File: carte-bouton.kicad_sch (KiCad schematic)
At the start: 46 parts, among them J1 Connecteur batterie, J14 Conn_ST_STDC14, J4 Conn_01x04, J5 Conn_01x03, J7 Conn_01x03, Q13 Q_NMOS_GDS, U1 LM317_SOT-223, U3 STM32F401RCTx, U4 LMR16020PDDA, Y1 Crystal_GND24

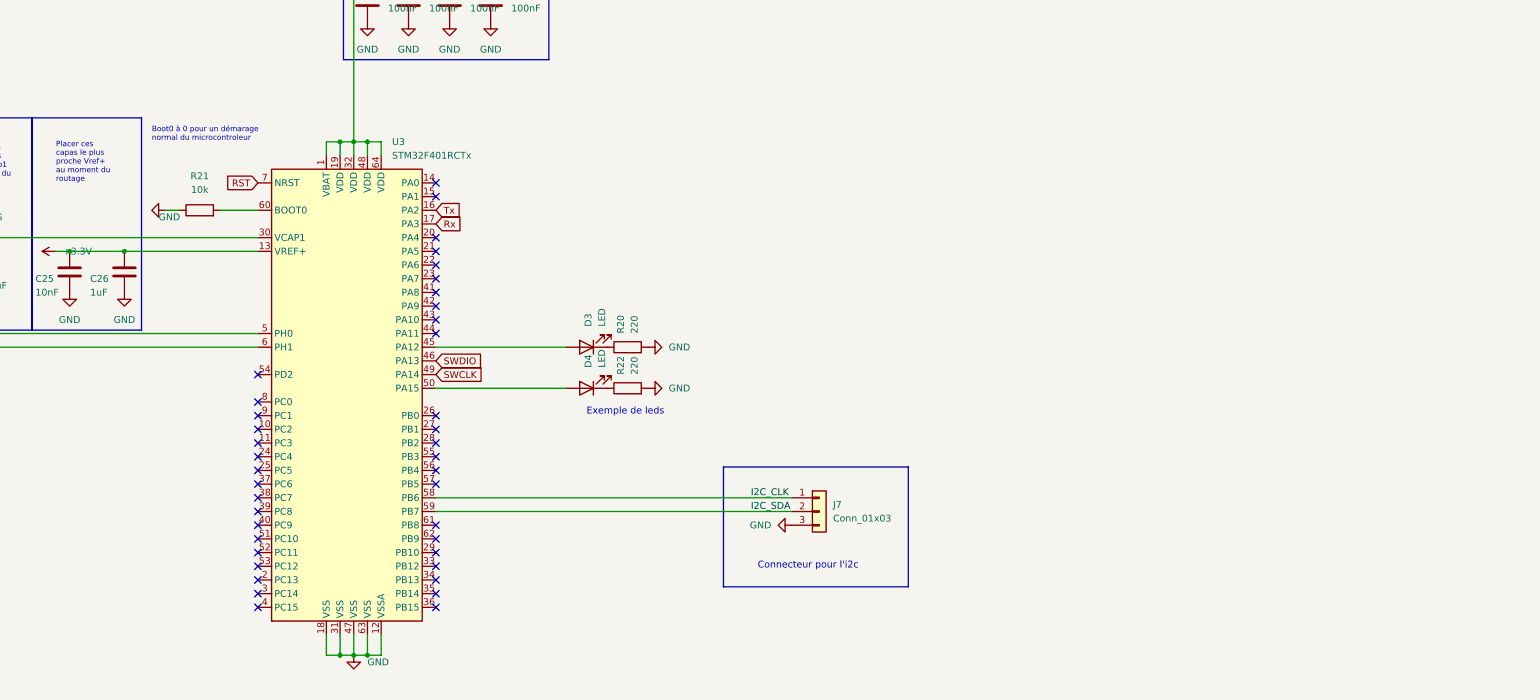
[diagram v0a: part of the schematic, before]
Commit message: Boutons, LEDs sans ecran
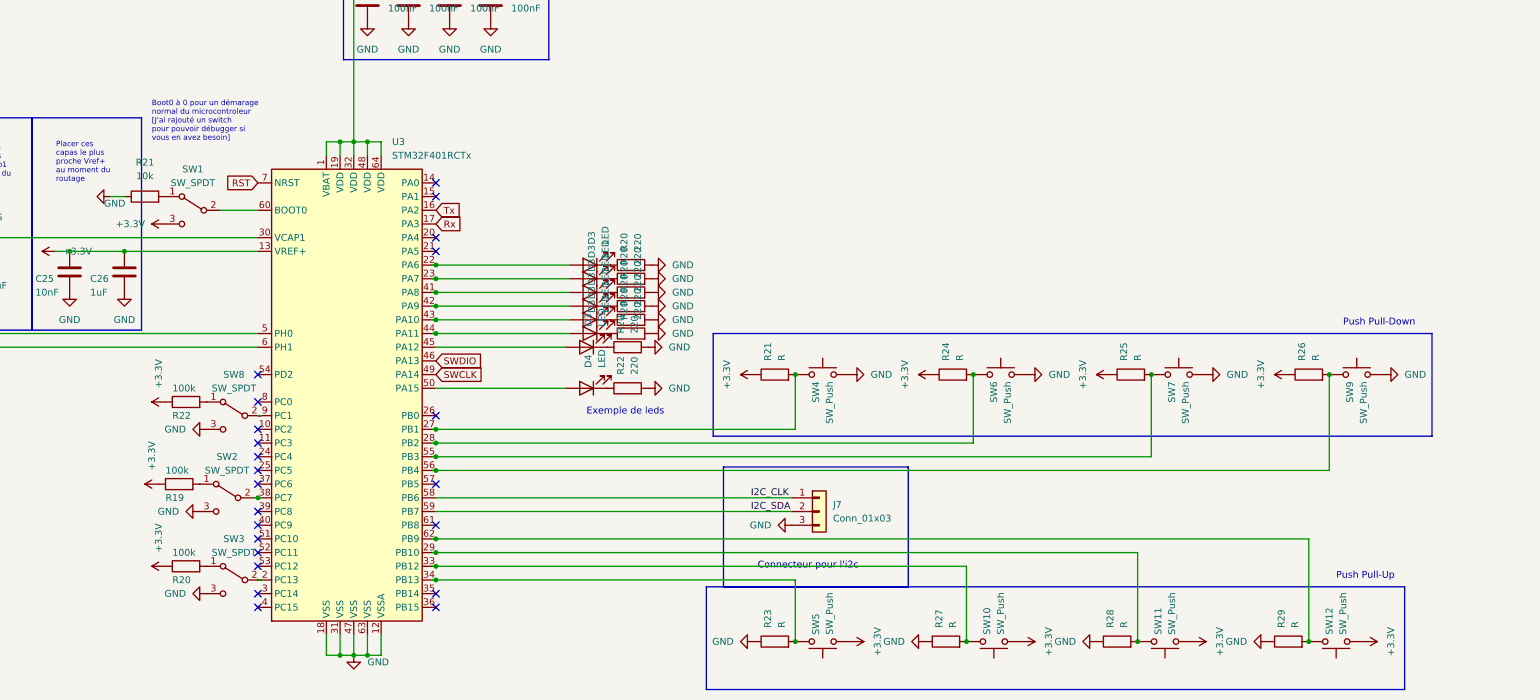
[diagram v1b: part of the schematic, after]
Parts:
- removed R21: 10k, Resistor_SMD:R_0805_2012Metric_Pad1.20x1.40mm_HandSolder, symbol Device:R
- added D3 (x6): LED, LED_SMD:LED_0805_2012Metric_Pad1.15x1.40mm_HandSolder, symbol Device:LED
- added R19, R20, R22: 100k, symbol Device:R
- added R20 (x6): 220, Resistor_SMD:R_0805_2012Metric_Pad1.20x1.40mm_HandSolder, symbol Device:R
- added R21, R23, R24, R25, R26, R27, R28, R29: R, symbol Device:R
- added R21: 10k, Resistor_SMD:R_0805_2012Metric_Pad1.20x1.40mm_HandSolder, symbol Device:R
- added SW1, SW2, SW3, SW8: SW_SPDT, symbol Switch:SW_SPDT
- added SW10, SW11, SW12, SW4, SW5, SW6, SW7, SW9: SW_Push, symbol Switch:SW_Push
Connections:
- net +3.3V: now also R19.1, R20.1, R21.1, R22.1, R24.1, R25.1, R26.1, SW1.3 (C), SW10.1, SW11.1, SW12.1, SW5.1
- net GND: now also R20.2, R20.2, R20.2, R20.2, R20.2, R20.2, R21.1, R23.1, R27.1, R28.1, R29.1, SW2.3 (C), SW3.3 (C), SW4.1, SW6.1, SW7.1, SW8.3 (C), SW9.1
- net at U3.60 (BOOT0): now also SW1.2 (B)
- net at U3.2 (PC13): now also SW3.2 (B)
- net at U3.22 (PA6): now also D3.2 (A)
- net at U3.23 (PA7): now also D3.2 (A)
- net at U3.27 (PB1): now also R21.2, SW4.2
- net at U3.28 (PB2): now also R24.2, SW6.2
- net at U3.29 (PB10): now also R28.2, SW11.2
- net at U3.33 (PB12): now also R27.2, SW10.2
- net at U3.34 (PB13): now also R23.2, SW5.2
- net at U3.38 (PC7): now also SW2.2 (B)
- net at U3.41 (PA8): now also D3.2 (A)
- net at U3.42 (PA9): now also D3.2 (A)
- net at U3.43 (PA10): now also D3.2 (A)
- net at U3.44 (PA11): now also D3.2 (A)
- net at U3.55 (PB3): now also R25.2, SW7.2
- net at U3.56 (PB4): now also R26.2, SW9.2
- net at U3.62 (PB9): now also R29.2, SW12.2
- net at U3.9 (PC1): now also SW8.2 (B)
- new net: R19.2, SW2.1 (A)
- new net: R20.2, SW3.1 (A)
- new net: D3.1 (K), R20.1 (x6)
- new net: R22.2, SW8.1 (A)
- new net: R21.2, SW1.1 (A)
- no-connect marks 45 -> 28
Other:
- note added: "Boot0 à 0 pour un démarage normal du microcontroleur [J'ai rajouté un switch pour pouvoir débugger si vous en avez besoin]"
- note added: "Push Pull-Down"
- note added: "Push Pull-Up"
- note removed: "Boot0 à 0 pour un démarage normal du microcontroleur"

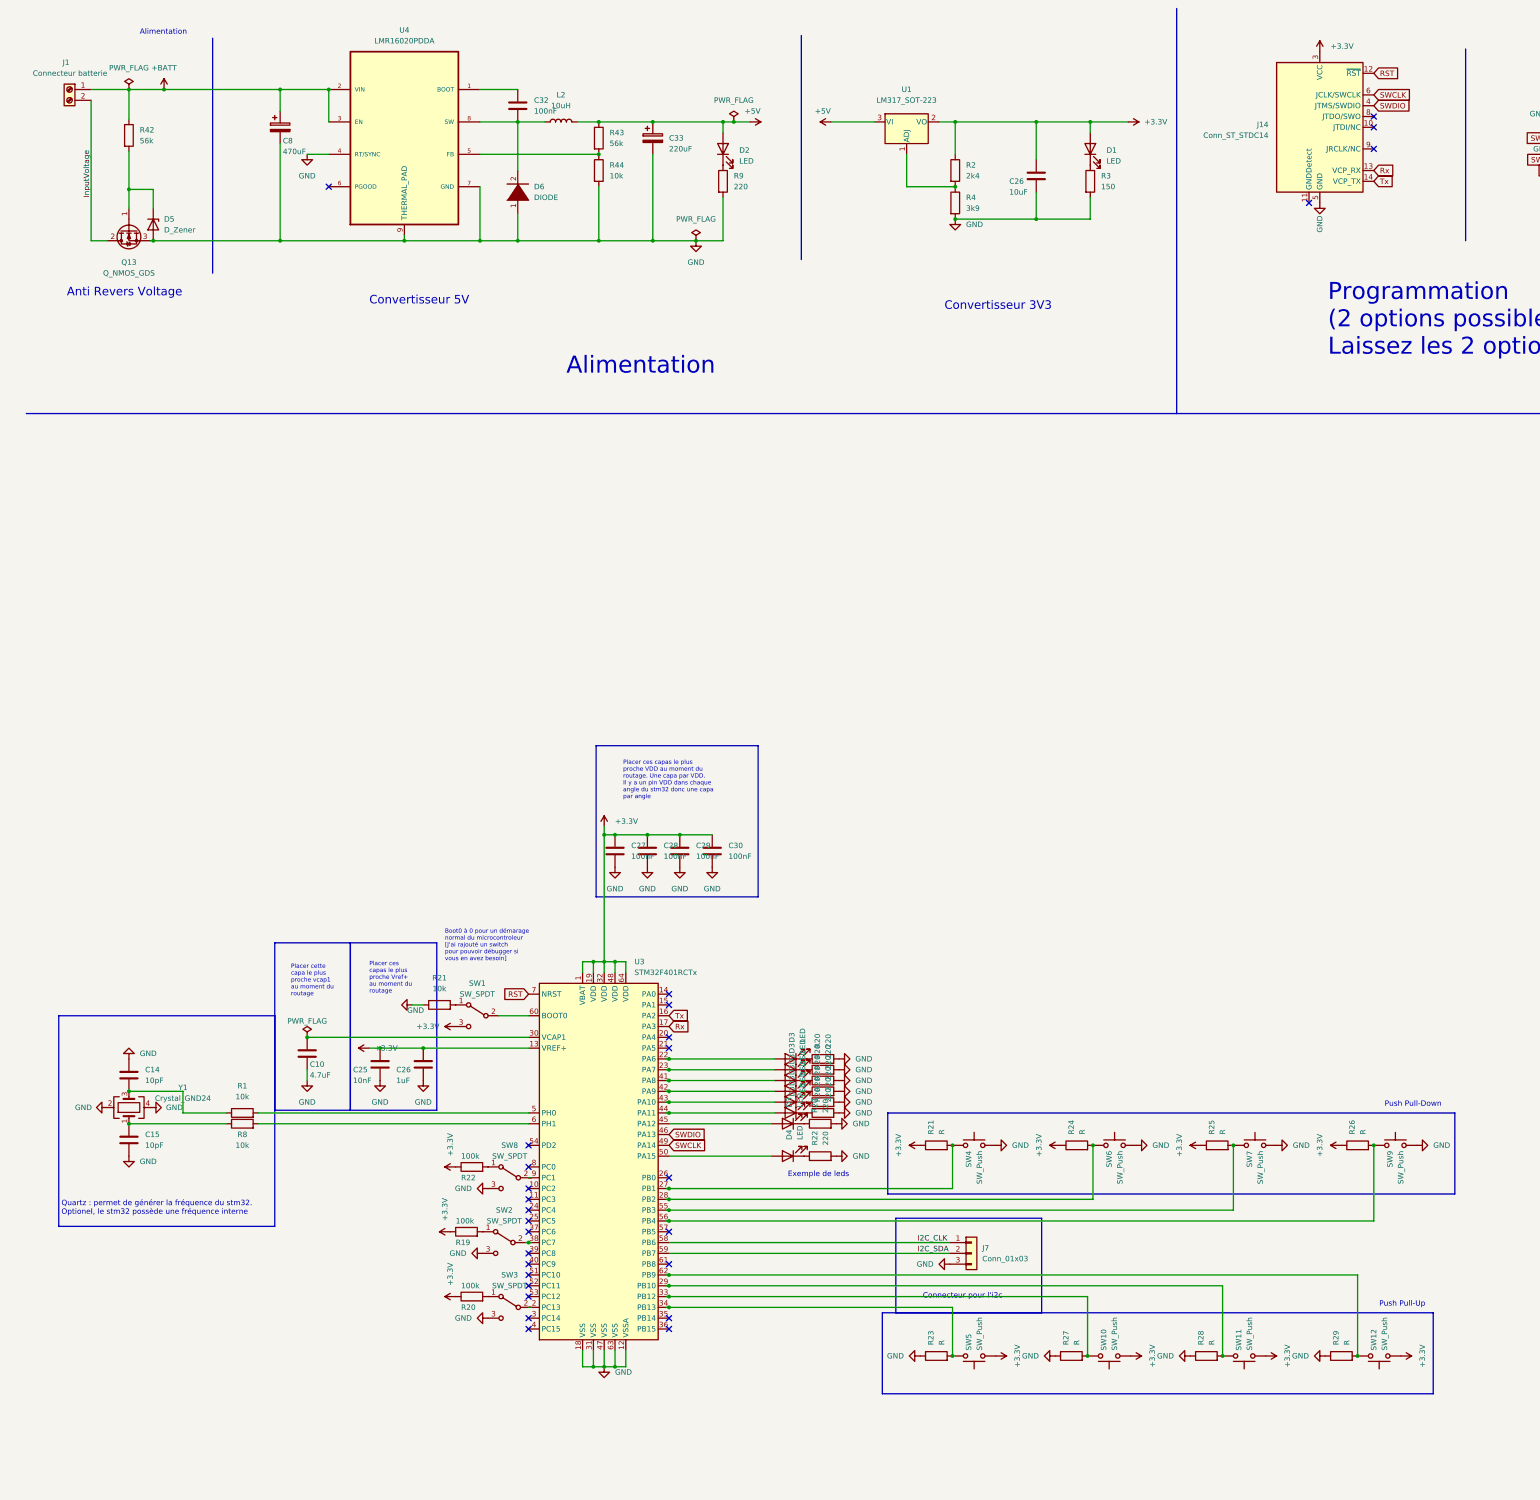
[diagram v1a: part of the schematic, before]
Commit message: modification schémas
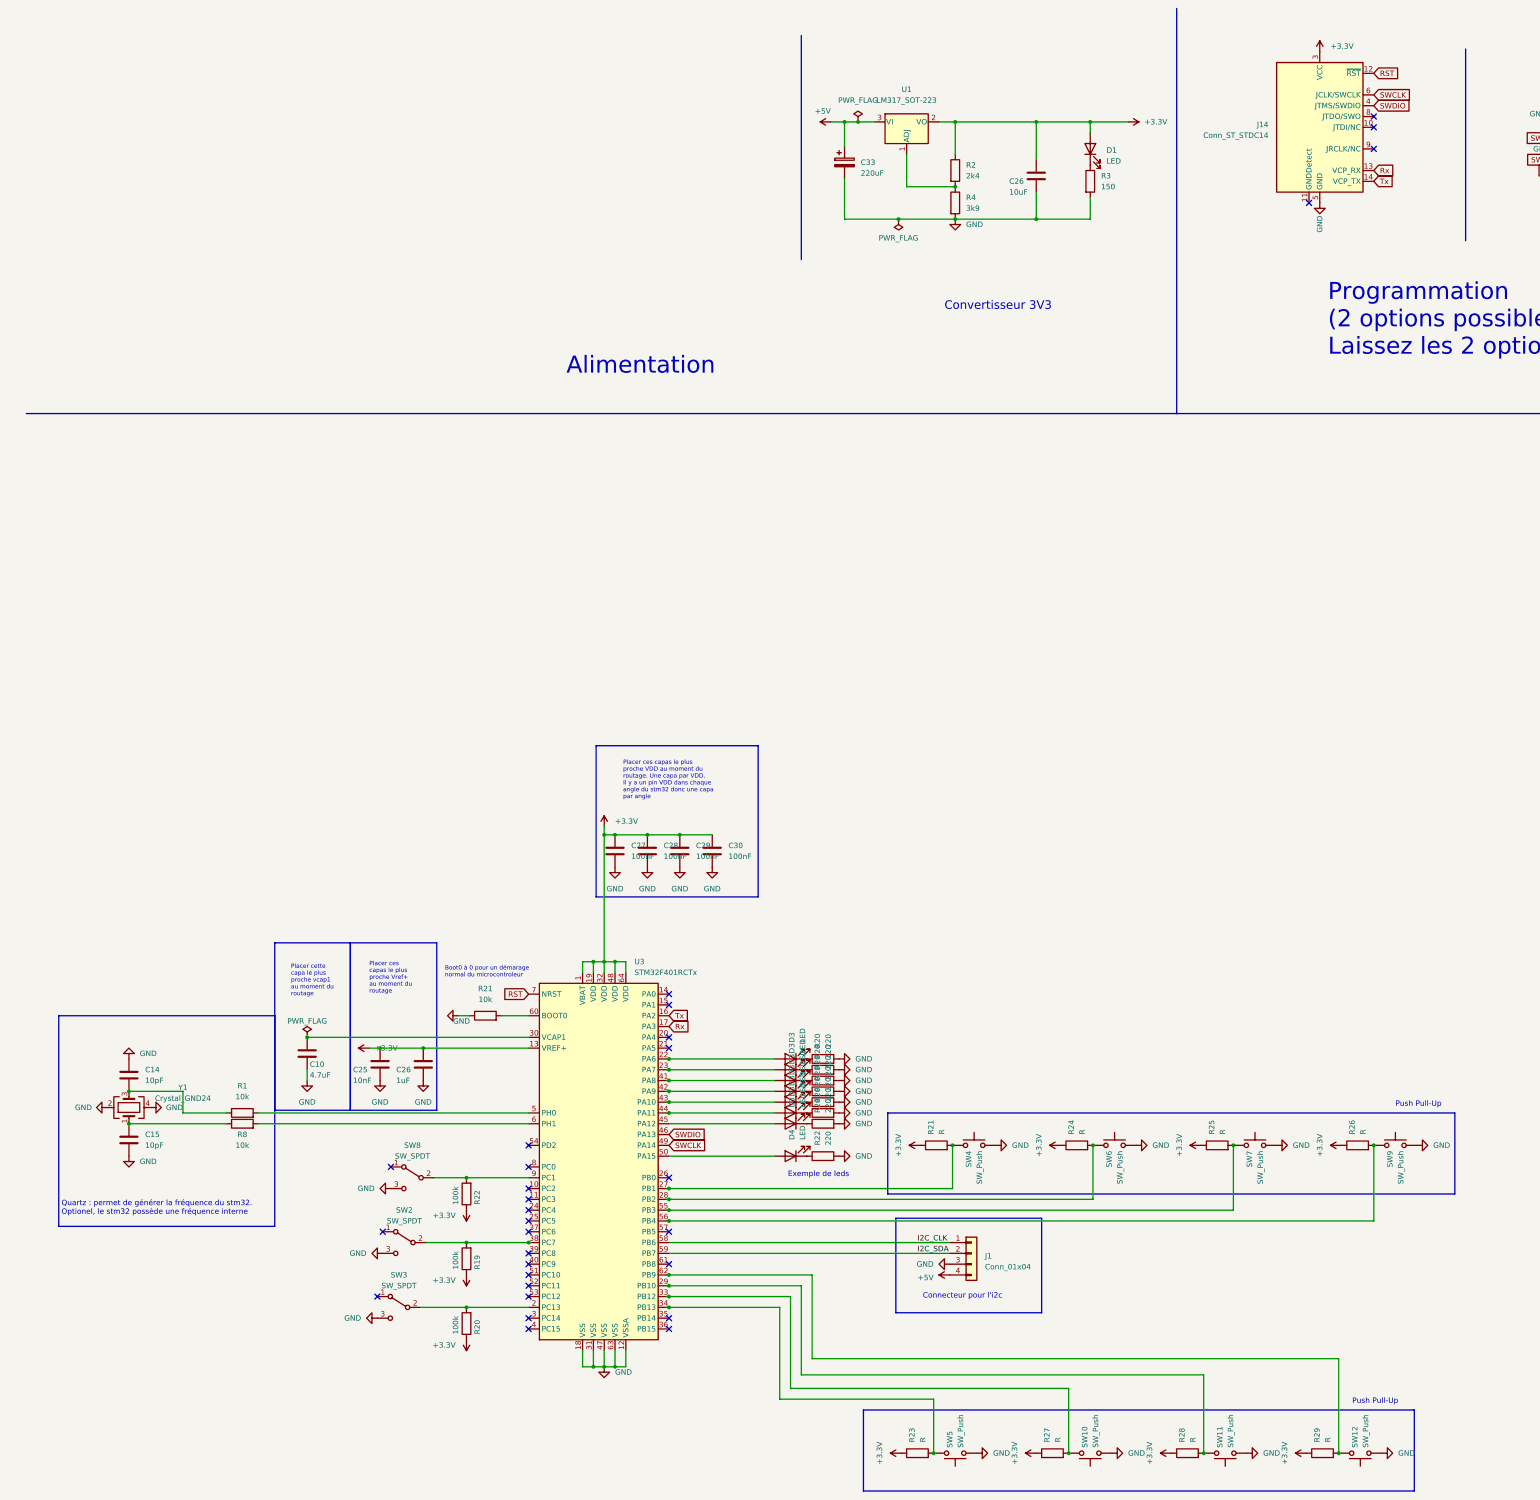
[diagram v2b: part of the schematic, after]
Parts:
- removed C32: 100nF, Capacitor_SMD:C_0805_2012Metric_Pad1.18x1.45mm_HandSolder, symbol Device:C
- removed C8: 470uF, Capacitor_SMD:CP_Elec_10x10.5, symbol Device:C_Polarized
- removed D2: LED, LED_SMD:LED_0805_2012Metric_Pad1.15x1.40mm_HandSolder, symbol Device:LED
- removed D5: D_Zener, Diode_SMD:D_SOD-123, symbol Device:D_Zener
- removed D6: DIODE, B170B:DIOM505270X240, symbol pspice:DIODE
- removed J1: Connecteur batterie, TerminalBlockBend:CUI_TBP01R1-508-02BE, symbol Connector:Screw_Terminal_01x02
- removed J7: Conn_01x03, Connector_JST:JST_XH_B3B-XH-A_1x03_P2.50mm_Vertical, symbol Connector_Generic:Conn_01x03
- removed L2: 10uH, IHLP2525CZER100M01:IND_IHLP_2525_CZ-M, symbol Device:L
- removed Q13: Q_NMOS_GDS, Package_TO_SOT_SMD:TO-252-2, symbol Device:Q_NMOS_GDS
- removed R42, R43: 56k, Resistor_SMD:R_0805_2012Metric_Pad1.20x1.40mm_HandSolder, symbol Device:R
- removed R44: 10k, Resistor_SMD:R_0805_2012Metric_Pad1.20x1.40mm_HandSolder, symbol Device:R
- removed R9: 220, Resistor_SMD:R_0805_2012Metric_Pad1.20x1.40mm_HandSolder, symbol Device:R
- removed SW1: SW_SPDT, symbol Switch:SW_SPDT
- removed U4: LMR16020PDDA, Package_SO:SOIC-8-1EP_3.9x4.9mm_P1.27mm_EP2.41x3.3mm, symbol LMR16020PDDA:LMR16020PDDA
- added J1: Conn_01x04, Connector_JST:JST_XH_B4B-XH-A_1x04_P2.50mm_Vertical, symbol Connector_Generic:Conn_01x04
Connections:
- net +3.3V: now also R23.1, R27.1, R28.1, R29.1; no longer SW10.1, SW11.1, SW12.1, SW5.1
- net +5V: now also J1.4 (Pin_4)
- net GND: now also SW10.1, SW11.1, SW12.1, SW5.1, J1.3 (Pin_3); no longer R23.1, R27.1, R28.1, R29.1
- net I2C_CLK: now also J1.1 (Pin_1)
- net I2C_SDA: now also J1.2 (Pin_2)
- net at R19.2: now also SW2.2 (B), U3.38 (PC7); no longer SW2.1 (A)
- net at SW3.1 (A): no longer R20.2
- net at SW3.2 (B), U3.2 (PC13): now also R20.2
- net at SW8.1 (A): no longer R22.2
- net at SW8.2 (B), U3.9 (PC1): now also R22.2
- net at R21.2: now also U3.60 (BOOT0)
- no-connect marks 28 -> 30
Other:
- note added: "Boot0 à 0 pour un démarage normal du microcontroleur"
- note removed: "Anti Revers Voltage"
- note removed: "Boot0 à 0 pour un démarage normal du microcontroleur [J'ai rajouté un switch pour pouvoir débugger si vous en avez besoin]"
- note removed: "Convertisseur 5V"
- note removed: "Push Pull-Down"
- moved on the sheet: D3, D4, R19, R20, R21, R22, R23, R27, R28, R29, SW10, SW11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
